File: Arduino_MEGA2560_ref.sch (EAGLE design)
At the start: 72 parts, among them IC1 MC33269ST-5.0T3, IC2 MC33269D-5.0, IC3 ATMEGA2560-16AU, IC4 ATMEGA8U2-MU, IC5 LM358D, IC6 LP2985-33DBVR, Q1 16MHz, Q2 16MHz, T2 FDN340P, X1 DC21MMX, Y1 16MHz, Y2 16MHz

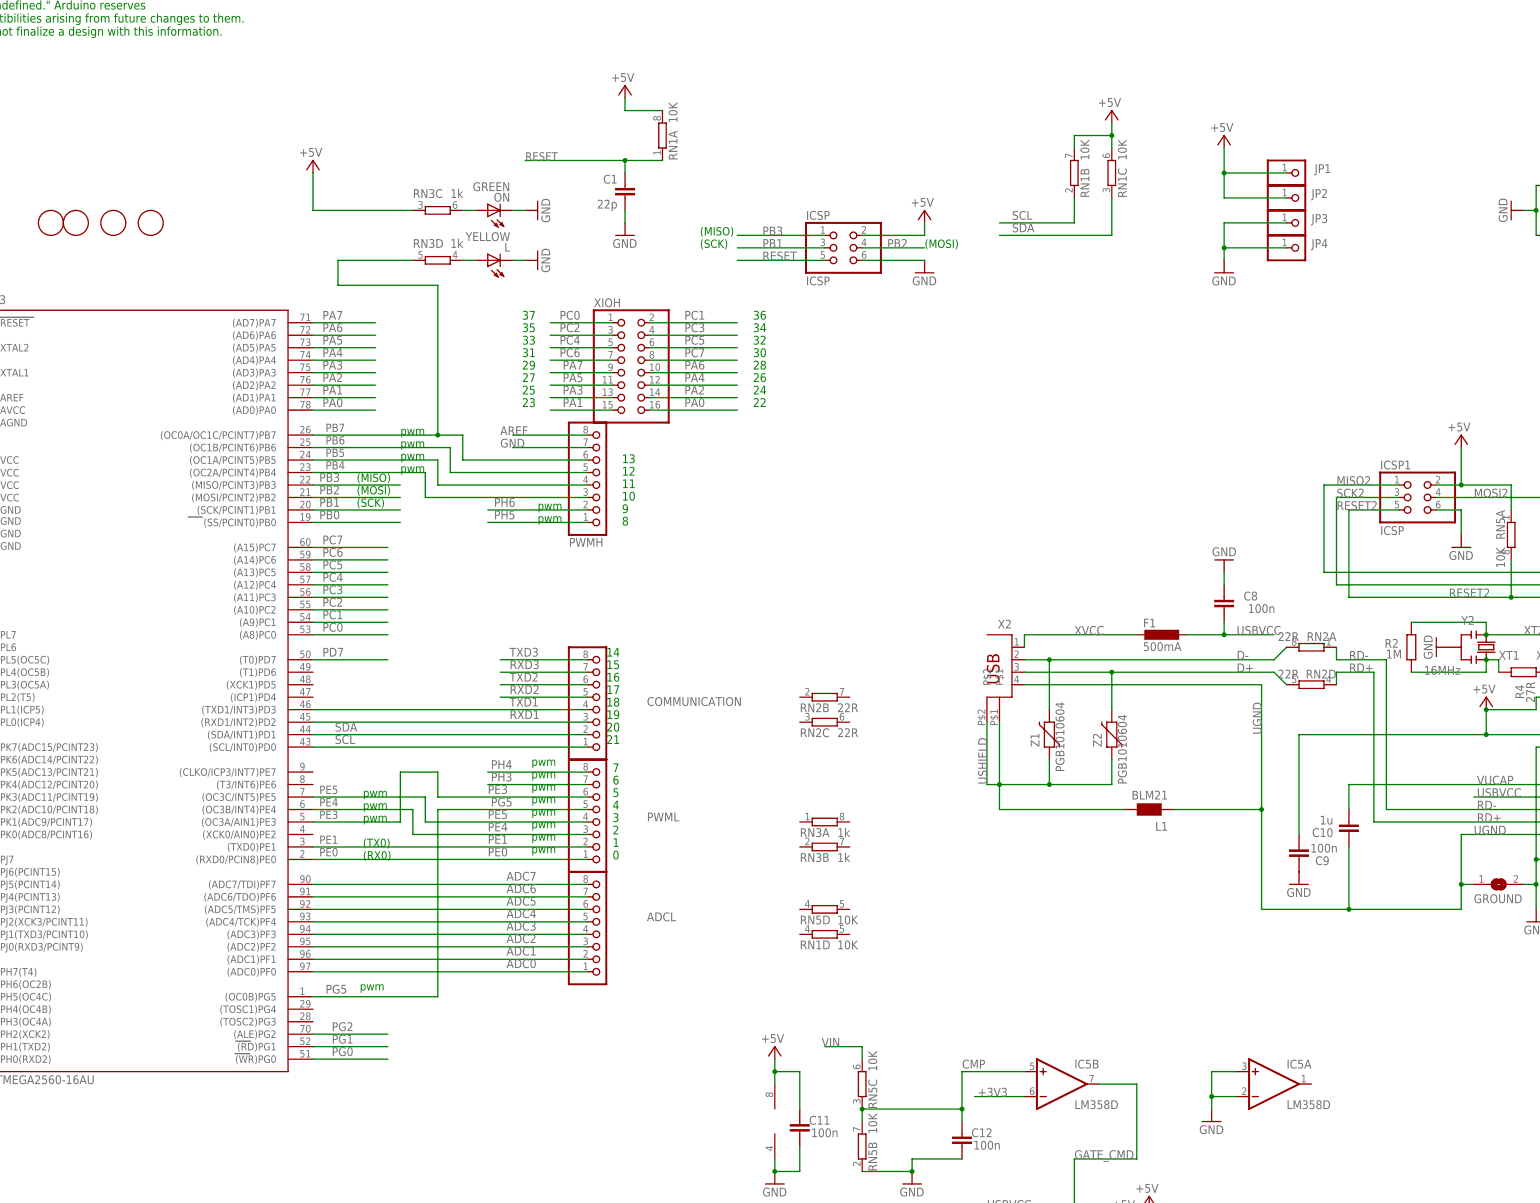
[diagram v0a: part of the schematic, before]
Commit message: Updated Arduino_MEGA2560_ref.sch
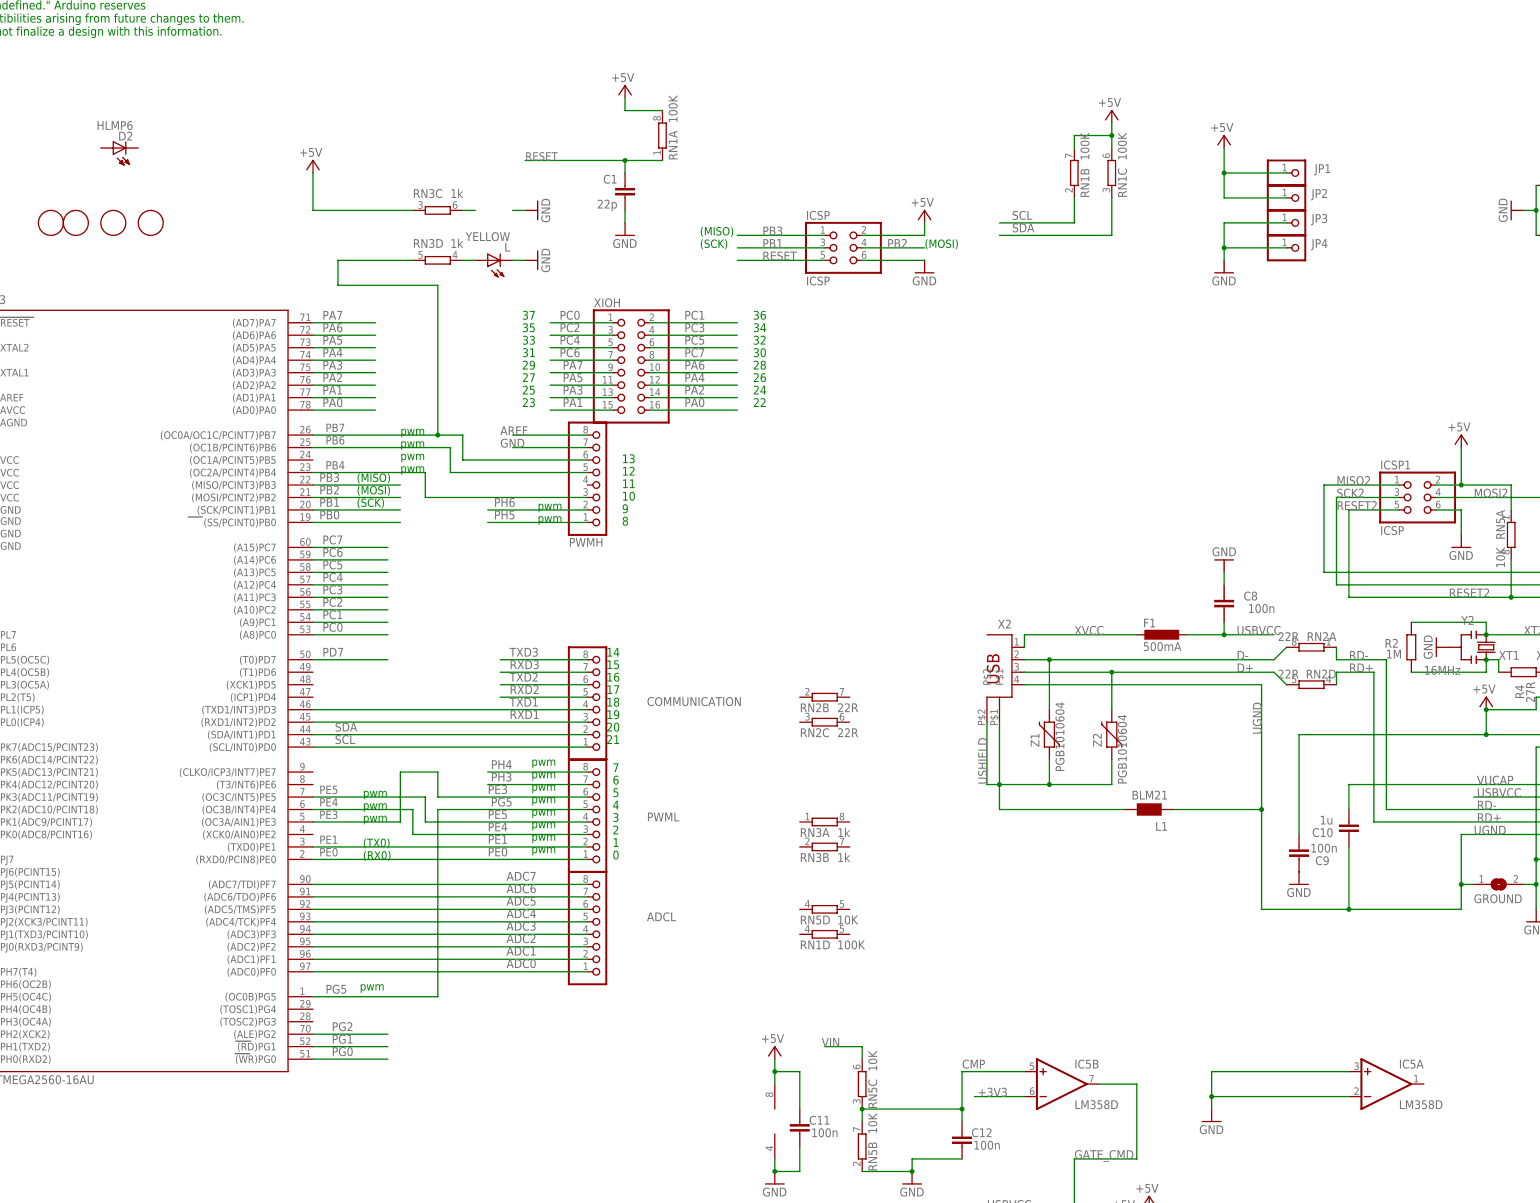
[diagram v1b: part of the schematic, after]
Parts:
- removed ON: GREEN, led:LEDCHIP-LED0805
- added D2: HLMP6, display-hp:HLMP6
- RN1: value 10K -> 100K
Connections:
- removed net PB5: IC3.(OC1A/PCINT5)PB5, PWMH.4
- net GND: no longer ON.C
- net N$3: no longer ON.A
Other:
- moved on the sheet: IC5A
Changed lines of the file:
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@@
 <?xml version="1.0" encoding="utf-8"?>
 <!DOCTYPE eagle SYSTEM "eagle.dtd">
-<eagle version="7.1.2">
+<eagle version="7.4.0">
 <drawing>
 <settings>
@@
 <grid distance="0.1" unitdist="inch" unit="inch" style="lines" multiple="1" display="no" altdistance="0.01" altunitdist="inch" altunit="inch"/>
 <layers>
-<layer number="1" name="Top" color="4" fill="1" visible="no" active="no"/>
-<layer number="2" name="Route2" color="1" fill="3" visible="no" active="no"/>
-<layer number="3" name="Route3" color="4" fill="3" visible="no" active="no"/>
-<layer number="14" name="Route14" color="1" fill="6" visible="no" active="no"/>
-<layer number="15" name="Route15" color="4" fill="6" visible="no" active="no"/>
-<layer number="16" name="Bottom" color="1" fill="1" visible="no" active="no"/>
-<layer number="17" name="Pads" color="2" fill="1" visible="no" active="no"/>
-<layer number="18" name="Vias" color="14" fill="1" visible="no" active="no"/>
-<layer number="19" name="Unrouted" color="6" fill="1" visible="no" active="no"/>
-<layer number="20" name="Dimension" color="15" fill="1" visible="no" active="no"/>
-<layer number="21" name="tPlace" color="7" fill="1" visible="no" active="no"/>
-<layer number="22" name="bPlace" color="7" fill="1" visible="no" active="no"/>
-<layer number="23" name="tOrigins" color="15" fill="1" visible="no" active="no"/>
-<layer number="24" name="bOrigins" color="15" fill="1" visible="no" active="no"/>
-<layer number="25" name="tNames" color="7" fill="1" visible="no" active="no"/>
-<layer number="26" name="bNames" color="7" fill="1" visible="no" active="no"/>
-<layer number="27" name="tValues" color="7" fill="1" visible="no" active="no"/>
-<layer number="28" name="bValues" color="7" fill="1" visible="no" active="no"/>
+<layer number="1" name="Top" color="4" fill="1" visible="yes" active="no"/>
+<layer number="2" name="Route2" color="1" fill="3" visible="yes" active="no"/>
+<layer number="3" name="Route3" color="4" fill="3" visible="yes" active="no"/>
+<layer number="14" name="Route14" color="1" fill="6" visible="yes" active="no"/>
+<layer number="15" name="Route15" color="4" fill="6" visible="yes" active="no"/>
+<layer number="16" name="Bottom" color="1" fill="1" visible="yes" active="no"/>
+<layer number="17" name="Pads" color="2" fill="1" visible="yes" active="no"/>
+<layer number="18" name="Vias" color="14" fill="1" visible="yes" active="no"/>
+<layer number="19" name="Unrouted" color="6" fill="1" visible="yes" active="no"/>
+<layer number="20" name="Dimension" color="15" fill="1" visible="yes" active="no"/>
+<layer number="21" name="tPlace" color="7" fill="1" visible="yes" active="no"/>
+<layer number="22" name="bPlace" color="7" fill="1" visible="yes" active="no"/>
+<layer number="23" name="tOrigins" color="15" fill="1" visible="yes" active="no"/>
+<layer number="24" name="bOrigins" color="15" fill="1" visible="yes" active="no"/>
+<layer number="25" name="tNames" color="7" fill="1" visible="yes" active="no"/>
+<layer number="26" name="bNames" color="7" fill="1" visible="yes" active="no"/>
+<layer number="27" name="tValues" color="7" fill="1" visible="yes" active="no"/>
+<layer number="28" name="bValues" color="7" fill="1" visible="yes" active="no"/>
 <layer number="29" name="tStop" color="2" fill="3" visible="no" active="no"/>
 <layer number="30" name="bStop" color="5" fill="6" visible="no" active="no"/>
@@
 <layer number="35" name="tGlue" color="7" fill="4" visible="no" active="no"/>
 <layer number="36" name="bGlue" color="7" fill="5" visible="no" active="no"/>
-<layer number="37" name="tTest" color="7" fill="1" visible="no" active="no"/>
-<layer number="38" name="bTest" color="7" fill="1" visible="no" active="no"/>
+<layer number="37" name="tTest" color="7" fill="1" visible="yes" active="no"/>
+<layer number="38" name="bTest" color="7" fill="1" visible="yes" active="no"/>
 <layer number="39" name="tKeepout" color="4" fill="11" visible="no" active="no"/>
 <layer number="40" name="bKeepout" color="1" fill="11" visible="no" active="no"/>
@@
 <layer number="44" name="Drills" color="7" fill="1" visible="no" active="no"/>
 <layer number="45" name="Holes" color="7" fill="1" visible="no" active="no"/>
-<layer number="46" name="Milling" color="3" fill="1" visible="no" active="no"/>
-<layer number="47" name="Measures" color="7" fill="1" visible="no" active="no"/>
-<layer number="48" name="Document" color="7" fill="1" visible="no" active="no"/>
-<layer number="49" name="Reference" color="13" fill="1" visible="no" active="no"/>
-<layer number="50" name="dxf" color="12" fill="1" visible="no" active="no"/>
-<layer number="51" name="tDocu" color="7" fill="1" visible="no" active="no"/>
-<layer number="52" name="bDocu" color="7" fill="1" visible="no" active="no"/>
-<layer number="53" name="tGND_GNDA" color="7" fill="1" visible="no" active="no"/>
-<layer number="54" name="bGND_GNDA" color="7" fill="1" visible="no" active="no"/>
-<layer number="56" name="wert" color="7" fill="1" visible="no" active="no"/>
+<layer number="46" name="Milling" color="3" fill="1" visible="yes" active="no"/>
+<layer number="47" name="Measures" color="7" fill="1" visible="yes" active="no"/>
+<layer number="48" name="Document" color="7" fill="1" visible="yes" active="no"/>
+<layer number="49" name="Reference" color="13" fill="1" visible="yes" active="no"/>
+<layer number="50" name="dxf" color="12" fill="1" visible="yes" active="no"/>
+<layer number="51" name="tDocu" color="7" fill="1" visible="yes" active="no"/>
+<layer number="52" name="bDocu" color="7" fill="1" visible="yes" active="no"/>
+<layer number="53" name="tGND_GNDA" color="7" fill="1" visible="yes" active="no"/>
+<layer number="54" name="bGND_GNDA" color="7" fill="1" visible="yes" active="no"/>
+<layer number="56" name="wert" color="7" fill="1" visible="yes" active="no"/>
 <layer number="91" name="Nets" color="2" fill="1" visible="yes" active="yes"/>
 <layer number="92" name="Busses" color="1" fill="1" visible="yes" active="yes"/>
@@
 <part name="GND12" library="supply1" deviceset="GND" device=""/>
 <part name="GND19" library="supply1" deviceset="GND" device=""/>
-<part name="ON" library="led" deviceset="LED" device="CHIP-LED0805" value="GREEN"/>
 <part name="GND14" library="supply1" deviceset="GND" device=""/>
 <part name="P+5" library="supply1" deviceset="+5V" device=""/>
@@
 <part name="RN4" library="resistor-dil" deviceset="4R-N" device="CAY16" value="1k"/>
 <part name="RN5" library="resistor-dil" deviceset="4R-N" device="CAT16" value="10K"/>
-<part name="RN1" library="resistor-dil" deviceset="4R-N" device="CAT16" value="10K"/>
+<part name="RN1" library="resistor-dil" deviceset="4R-N" device="CAT16" value="100K"/>
 <part name="RN3" library="resistor-dil" deviceset="4R-N" device="CAY16" value="1k"/>
 <part name="U$5" library="SmartPrj" deviceset="FIDUCIALMOUNT" device=""/>
@@
 <part name="R3" library="SmartPrj" deviceset="R-EU_" device="R0603" value="27R"/>
 <part name="R4" library="SmartPrj" deviceset="R-EU_" device="R0603" value="27R"/>
+<part name="D2" library="display-hp" deviceset="HLMP6" device=""/>
 </parts>
 <sheets>
@@
 <instance part="GND12" gate="1" x="43.18" y="-22.86" rot="R90"/>
 <instance part="GND19" gate="1" x="12.7" y="144.78"/>
-<instance part="ON" gate="G$1" x="210.82" y="160.02" rot="R90"/>
 <instance part="GND14" gate="1" x="220.98" y="160.02" rot="R90"/>
 <instance part="P+5" gate="1" x="175.26" y="170.18" smashed="yes">
@@
 <attribute name="VALUE" x="320.675" y="-64.135" size="1.778" layer="96" rot="MR180"/>
 </instance>
-<instance part="IC5" gate="A" x="370.84" y="-17.78" smashed="yes">
-<attribute name="NAME" x="373.38" y="-14.605" size="1.778" layer="95"/>
-<attribute name="VALUE" x="373.38" y="-22.86" size="1.778" layer="96"/>
+<instance part="IC5" gate="A" x="393.7" y="-17.78" smashed="yes">
+<attribute name="NAME" x="396.24" y="-14.605" size="1.778" layer="95"/>
+<attribute name="VALUE" x="396.24" y="-22.86" size="1.778" layer="96"/>
 </instance>
 <instance part="IC5" gate="B" x="327.66" y="-17.78"/>
@@
 <attribute name="VALUE" x="422.148" y="64.135" size="1.778" layer="96" rot="R270"/>
 </instance>
+<instance part="D2" gate="A" x="137.16" y="172.72" rot="R90"/>
 </instances>
 <busses>
@@
 <wire x1="218.44" y1="160.02" x2="215.9" y2="160.02" width="0.1524" layer="91"/>
 <pinref part="GND14" gate="1" pin="GND"/>
-<pinref part="ON" gate="G$1" pin="C"/>
 </segment>
 <segment>
@@
 </segment>
 <segment>
-<wire x1="363.22" y1="-15.24" x2="358.14" y2="-15.24" width="0.1524" layer="91"/>
+<wire x1="386.08" y1="-15.24" x2="358.14" y2="-15.24" width="0.1524" layer="91"/>
 <wire x1="358.14" y1="-15.24" x2="358.14" y2="-20.32" width="0.1524" layer="91"/>
-<wire x1="358.14" y1="-20.32" x2="363.22" y2="-20.32" width="0.1524" layer="91"/>
+<wire x1="358.14" y1="-20.32" x2="386.08" y2="-20.32" width="0.1524" layer="91"/>
 <wire x1="358.14" y1="-22.86" x2="358.14" y2="-20.32" width="0.1524" layer="91"/>
 <junction x="358.14" y="-20.32"/>
@@
 <segment>
 <wire x1="208.28" y1="160.02" x2="205.74" y2="160.02" width="0.1524" layer="91"/>
-<pinref part="ON" gate="G$1" pin="A"/>
 <pinref part="RN3" gate="C" pin="2"/>
 </segment>
@@
 </segment>
 </net>
-<net name="PB5" class="0">
-<segment>
-<wire x1="175.26" y1="109.22" x2="200.66" y2="109.22" width="0.1524" layer="91"/>
-<wire x1="231.14" y1="104.14" x2="200.66" y2="104.14" width="0.1524" layer="91"/>
-<wire x1="200.66" y1="104.14" x2="200.66" y2="109.22" width="0.1524" layer="91"/>
-<label x="177.8" y="109.855" size="1.6764" layer="95"/>
-<pinref part="IC3" gate="1" pin="(OC1A/PCINT5)PB5"/>
-<pinref part="PWMH" gate="A" pin="4"/>
-</segment>
-</net>
